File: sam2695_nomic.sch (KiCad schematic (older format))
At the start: 31 parts, among them J1 HeadphoneOut, J2 MicIn, U3 SAM2695, X1 12MHz

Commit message: UPDATEUPDATES!!!
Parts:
- removed C20: 1µfT, Capacitors_SMD:C_0805_HandSoldering, symbol Cap
- removed C21: 220pF, Capacitors_SMD:C_0805_HandSoldering, symbol C_Small
- removed J1: HeadphoneOut, Zetaohm:Switchcraft_3.5mm_SMD_Stereo, symbol Headphones-RESCUE-afx-01
- removed J2: MicIn, Zetaohm:Switchcraft_3.5mm_SMD_Stereo, symbol Headphones-RESCUE-afx-01
- removed R7: 4.7k, Resistors_SMD:R_0805_HandSoldering, symbol Resistor
- added U9: 3_pin_stereo, symbol 3_pin_stereo
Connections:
- net labels removed: VCC
- wire segments 136 -> 122
- no-connect marks 12 -> 10
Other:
- moved on the sheet: C12, R5
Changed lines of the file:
@@
 LIBS:contrib
 LIBS:valves
+LIBS:afx-01-cache
 EELAYER 25 0
 EELAYER END
@@
 $EndComp
 $Comp
-L VCC #PWR033
-U 1 1 55727FD6
-P 7650 4400
-F 0 "#PWR033" H 7650 4250 50  0001 C CNN
-F 1 "VCC" H 7650 4550 50  0000 C CNN
-F 2 "" H 7650 4400 60  0000 C CNN
-F 3 "" H 7650 4400 60  0000 C CNN
-	1    7650 4400
-	1    0    0    -1
-$EndComp
-$Comp
 L Cap C5
 U 1 1 55728143
@@
 $EndComp
 $Comp
-L VCC #PWR034
-U 1 1 55728291
-P 4250 3200
-F 0 "#PWR034" H 4250 3050 50  0001 C CNN
-F 1 "VCC" H 4250 3350 50  0000 C CNN
-F 2 "" H 4250 3200 60  0000 C CNN
-F 3 "" H 4250 3200 60  0000 C CNN
-	1    4250 3200
-	1    0    0    -1
-$EndComp
-$Comp
 L Cap C12
 U 1 1 55728514
-P 5800 2100
-F 0 "C12" V 5850 2200 39  0000 L CNN
-F 1 "100µfT" V 5650 2100 39  0000 L CNN
-F 2 "Capacitors_SMD:C_0805_HandSoldering" H 5710 2030 60  0001 C CNN
-F 3 "" H 5800 2100 60  0000 C CNN
-	1    5800 2100
+P 6100 1900
+F 0 "C12" V 6150 2000 39  0000 L CNN
+F 1 "100µfT" V 5950 1900 39  0000 L CNN
+F 2 "Capacitors_SMD:C_0805_HandSoldering" H 6010 1830 60  0001 C CNN
+F 3 "" H 6100 1900 60  0000 C CNN
+	1    6100 1900
 	0    -1   -1   0
 $EndComp
@@
 $EndComp
 $Comp
-L VCC #PWR035
-U 1 1 5572872F
-P 8050 3250
-F 0 "#PWR035" H 8050 3100 50  0001 C CNN
-F 1 "VCC" H 8050 3400 50  0000 C CNN
-F 2 "" H 8050 3250 60  0000 C CNN
-F 3 "" H 8050 3250 60  0000 C CNN
-	1    8050 3250
-	1    0    0    -1
-$EndComp
-$Comp
 L INDUCTOR_SMALL L1
 U 1 1 557287C4
@@
 L Resistor R5
 U 1 1 5572AB09
-P 7150 2200
-F 0 "R5" H 7300 2250 50  0000 C CNN
-F 1 "47k" H 7300 2150 50  0000 C CNN
-F 2 "Resistors_SMD:R_0805_HandSoldering" V 7080 2200 30  0001 C CNN
-F 3 "" H 7150 2200 30  0000 C CNN
-	1    7150 2200
-	1    0    0    -1
-$EndComp
-$Comp
-L Headphones-RESCUE-afx-01 J1
-U 1 1 5572B19C
-P 7750 1750
-F 0 "J1" H 7770 1900 60  0000 C CNN
-F 1 "HeadphoneOut" H 8000 1550 60  0000 C CNN
-F 2 "Zetaohm:Switchcraft_3.5mm_SMD_Stereo" H 7750 1750 60  0001 C CNN
-F 3 "" H 7750 1750 60  0000 C CNN
-	1    7750 1750
-	1    0    0    -1
-$EndComp
-$Comp
-L Headphones-RESCUE-afx-01 J2
-U 1 1 5572B6E6
-P 9050 2850
-F 0 "J2" H 9070 3000 60  0000 C CNN
-F 1 "MicIn" H 9150 2650 60  0000 C CNN
-F 2 "Zetaohm:Switchcraft_3.5mm_SMD_Stereo" H 9050 2850 60  0001 C CNN
-F 3 "" H 9050 2850 60  0000 C CNN
-	1    9050 2850
-	1    0    0    -1
-$EndComp
-$Comp
-L Cap C20
-U 1 1 5572BA3E
-P 7850 2750
-F 0 "C20" V 7900 2850 39  0000 L CNN
-F 1 "1µfT" V 7900 2250 39  0000 L CNN
-F 2 "Capacitors_SMD:C_0805_HandSoldering" H 7760 2680 60  0001 C CNN
-F 3 "" H 7850 2750 60  0000 C CNN
-	1    7850 2750
-	0    -1   -1   0
-$EndComp
-$Comp
-L C_Small C21
-U 1 1 5572BAE5
-P 8300 2850
-F 0 "C21" H 8450 2850 50  0000 L CNN
-F 1 "220pF" H 8350 2950 50  0000 L CNN
-F 2 "Capacitors_SMD:C_0805_HandSoldering" H 8300 2850 60  0001 C CNN
-F 3 "" H 8300 2850 60  0000 C CNN
-	1    8300 2850
-	-1   0    0    1
-$EndComp
-$Comp
-L Resistor R7
-U 1 1 5572BB93
-P 8500 3000
-F 0 "R7" H 8650 3050 50  0000 C CNN
-F 1 "4.7k" H 8650 2950 50  0000 C CNN
-F 2 "Resistors_SMD:R_0805_HandSoldering" V 8430 3000 30  0001 C CNN
-F 3 "" H 8500 3000 30  0000 C CNN
-	1    8500 3000
+P 6650 2000
+F 0 "R5" H 6800 2050 50  0000 C CNN
+F 1 "47k" H 6800 1950 50  0000 C CNN
+F 2 "Resistors_SMD:R_0805_HandSoldering" V 6580 2000 30  0001 C CNN
+F 3 "" H 6650 2000 30  0000 C CNN
+	1    6650 2000
 	1    0    0    -1
 $EndComp
 NoConn ~ 5350 3100
-NoConn ~ 7650 1700
-NoConn ~ 7650 1750
 Text HLabel 3550 2900 0    60   Input ~ 0
 MIDIIN
@@
 NoConn ~ 4650 4000
 $Comp
+L GNDA #PWR035
+U 1 1 561F077A
+P 6650 2350
+F 0 "#PWR035" H 6650 2100 50  0001 C CNN
+F 1 "GNDA" H 6650 2200 50  0000 C CNN
+F 2 "" H 6650 2350 60  0000 C CNN
+F 3 "" H 6650 2350 60  0000 C CNN
+	1    6650 2350
+	1    0    0    -1
+$EndComp
+$Comp
 L GNDA #PWR036
-U 1 1 561F077A
-P 7150 2400
-F 0 "#PWR036" H 7150 2150 50  0001 C CNN
-F 1 "GNDA" H 7150 2250 50  0000 C CNN
-F 2 "" H 7150 2400 60  0000 C CNN
-F 3 "" H 7150 2400 60  0000 C CNN
-	1    7150 2400
-	1    0    0    -1
-$EndComp
-$Comp
-L GNDA #PWR037
-U 1 1 561F07E6
-P 8850 3200
-F 0 "#PWR037" H 8850 2950 50  0001 C CNN
-F 1 "GNDA" H 8850 3050 50  0000 C CNN
-F 2 "" H 8850 3200 60  0000 C CNN
-F 3 "" H 8850 3200 60  0000 C CNN
-	1    8850 3200
-	1    0    0    -1
-$EndComp
-$Comp
-L GNDA #PWR038
-U 1 1 561F086A
-P 6250 1900
-F 0 "#PWR038" H 6250 1650 50  0001 C CNN
-F 1 "GNDA" H 6250 1750 50  0000 C CNN
-F 2 "" H 6250 1900 60  0000 C CNN
-F 3 "" H 6250 1900 60  0000 C CNN
-	1    6250 1900
-	1    0    0    -1
-$EndComp
-$Comp
-L GNDA #PWR039
 U 1 1 561F08CF
 P 8000 3600
-F 0 "#PWR039" H 8000 3350 50  0001 C CNN
+F 0 "#PWR036" H 8000 3350 50  0001 C CNN
 F 1 "GNDA" H 8000 3450 50  0000 C CNN
 F 2 "" H 8000 3600 60  0000 C CNN
@@
 $EndComp
 $Comp
-L GNDA #PWR040
+L GNDA #PWR037
 U 1 1 561F0AFD
 P 5400 5500
-F 0 "#PWR040" H 5400 5250 50  0001 C CNN
+F 0 "#PWR037" H 5400 5250 50  0001 C CNN
 F 1 "GNDA" H 5400 5350 50  0000 C CNN
 F 2 "" H 5400 5500 60  0000 C CNN
@@
 $EndComp
 $Comp
-L +3V3 #PWR041
+L +3V3 #PWR038
 U 1 1 561F0D6B
 P 4000 3600
-F 0 "#PWR041" H 4000 3450 50  0001 C CNN
+F 0 "#PWR038" H 4000 3450 50  0001 C CNN
 F 1 "+3V3" H 4000 3740 50  0000 C CNN
 F 2 "" H 4000 3600 60  0000 C CNN
@@
 Connection ~ 6800 4200
 Wire Wire Line
-	4500 5350 4500 5100
-Wire Wire Line
-	4500 5100 4650 5100
+	4550 5350 4550 4500
+Wire Wire Line
+	4550 5100 4650 5100
 Connection ~ 7450 4350
 Wire Wire Line
-	4650 4500 4550 4500
-Wire Wire Line
-	4550 4500 4550 5100
+	4550 4500 4650 4500
 Wire Wire Line
 	4550 4600 4650 4600
@@
 Wire Wire Line
 	7650 4450 7650 4400
-Connection ~ 4500 5350
+Connection ~ 4550 5350
 Wire Wire Line
 	4650 3250 4250 3250
@@
 	5550 2900 5350 2900
 Wire Wire Line
-	5550 2100 5550 2900
-Wire Wire Line
-	5550 2100 5700 2100
+	5550 1900 5550 2900
+Wire Wire Line
+	5550 1900 6000 1900
 Wire Wire Line
 	5400 1650 5400 3000
@@
 	5850 1650 7650 1650
 Wire Wire Line
-	6250 1850 6250 1900
-Wire Wire Line
-	5850 2100 7500 2100
-Wire Wire Line
-	7150 2300 7150 2400
+	6250 1850 6250 2200
+Wire Wire Line
+	6150 1900 7050 1900
+Wire Wire Line
+	6650 2100 6650 2350
 Connection ~ 6250 1650
 Wire Wire Line
-	7500 2100 7500 1800
-Wire Wire Line
-	7500 1800 7650 1800
-Connection ~ 7150 2100
-Wire Wire Line
-	7650 1850 7600 1850
-Wire Wire Line
-	7600 1850 7600 2350
-Wire Wire Line
-	7600 2350 7150 2350
-Connection ~ 7150 2350
-Wire Wire Line
-	5350 3200 5800 3200
-Wire Wire Line
-	5800 3200 5800 2750
-Wire Wire Line
-	5800 2750 7750 2750
-Wire Wire Line
-	8950 2900 8500 2900
-Wire Wire Line
-	8850 2950 8950 2950
-Wire Wire Line
-	8850 2750 8850 3200
-Wire Wire Line
-	8300 3100 8850 3100
-Connection ~ 8850 3100
-Wire Wire Line
-	8300 3100 8300 2950
-Connection ~ 8500 3100
-Wire Wire Line
-	7900 2750 8500 2750
-Wire Wire Line
-	8500 2750 8500 2900
-Connection ~ 8300 2750
-Wire Wire Line
-	8850 2750 8950 2750
-Connection ~ 8850 2950
-Wire Wire Line
-	8950 2800 8850 2800
-Connection ~ 8850 2800
-Wire Wire Line
-	8950 2850 8850 2850
-Connection ~ 8850 2850
+	7050 1900 7050 1750
+Wire Wire Line
+	7050 1750 7650 1750
+Connection ~ 6650 1900
+Wire Wire Line
+	7650 1850 7200 1850
+Wire Wire Line
+	7200 1850 7200 2200
+Wire Wire Line
+	7200 2200 6250 2200
+Connection ~ 6650 2200
 Wire Wire Line
 	3550 2900 3850 2900
@@
 Connection ~ 4000 4250
 Connection ~ 4000 4150
+$Comp
+L 3_pin_stereo U9
+U 1 1 5622F23F
+P 7750 1750
+F 0 "U9" H 7770 1900 60  0000 C CNN
+F 1 "3_pin_stereo" H 7920 1600 60  0000 C CNN
+F 2 "" H 7750 1750 60  0000 C CNN
+F 3 "" H 7750 1750 60  0000 C CNN
+	1    7750 1750
+	1    0    0    -1
+$EndComp
+$Comp
+L +3V3 #PWR039
+U 1 1 5622FC98
+P 4250 3200
+F 0 "#PWR039" H 4250 3050 50  0001 C CNN
+F 1 "+3V3" H 4250 3340 50  0000 C CNN
+F 2 "" H 4250 3200 60  0000 C CNN
+F 3 "" H 4250 3200 60  0000 C CNN
+	1    4250 3200
+	1    0    0    -1
+$EndComp
+$Comp
+L +3V3 #PWR040
+U 1 1 5622FD5B
+P 7650 4400
+F 0 "#PWR040" H 7650 4250 50  0001 C CNN
+F 1 "+3V3" H 7650 4540 50  0000 C CNN
+F 2 "" H 7650 4400 60  0000 C CNN
+F 3 "" H 7650 4400 60  0000 C CNN
+	1    7650 4400
+	1    0    0    -1
+$EndComp
+$Comp
+L +3V3 #PWR041
+U 1 1 5622FDB4
+P 8050 3250
+F 0 "#PWR041" H 8050 3100 50  0001 C CNN
+F 1 "+3V3" H 8050 3390 50  0000 C CNN
+F 2 "" H 8050 3250 60  0000 C CNN
+F 3 "" H 8050 3250 60  0000 C CNN
+	1    8050 3250
+	1    0    0    -1
+$EndComp
 $EndSCHEMATC

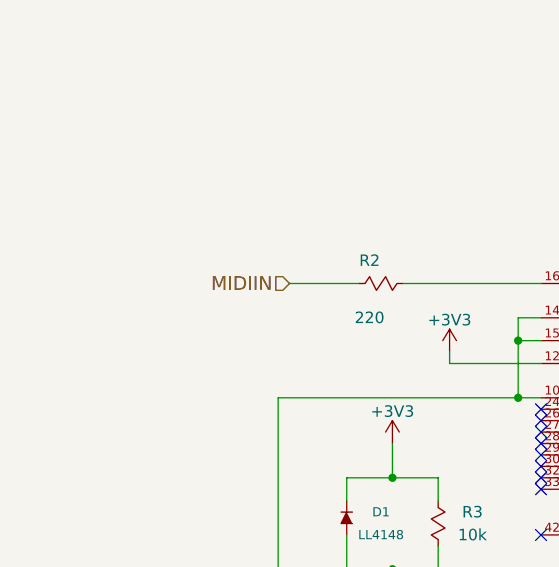
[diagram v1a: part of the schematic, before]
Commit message: Added Touch Capacitive Panel
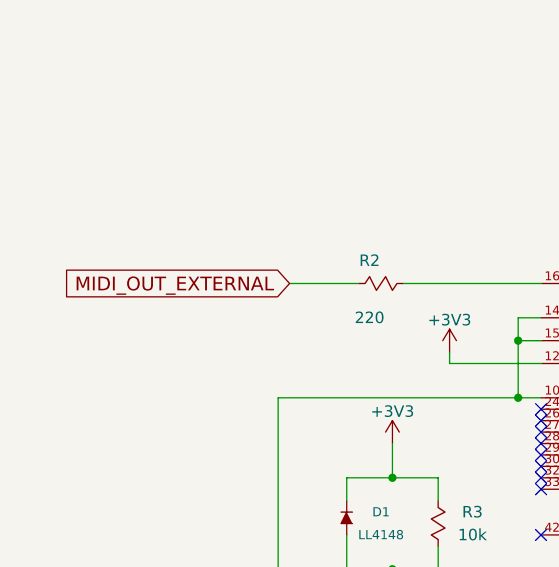
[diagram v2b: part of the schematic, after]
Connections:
- net MIDIIN renamed MIDI_OUT_EXTERNAL
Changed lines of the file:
@@
 $Descr A4 11693 8268
 encoding utf-8
-Sheet 3 7
+Sheet 3 8
 Title ""
 Date ""
@@
 $EndComp
 NoConn ~ 5350 3100
-Text HLabel 3550 2900 0    60   Input ~ 0
-MIDIIN
 $Comp
 L Resistor R2
@@
 NoConn ~ 4650 4000
 $Comp
-L GNDA #PWR035
+L GNDA #PWR037
 U 1 1 561F077A
 P 6650 2350
-F 0 "#PWR035" H 6650 2100 50  0001 C CNN
+F 0 "#PWR037" H 6650 2100 50  0001 C CNN
 F 1 "GNDA" H 6650 2200 50  0000 C CNN
 F 2 "" H 6650 2350 60  0000 C CNN
@@
 $EndComp
 $Comp
-L GNDA #PWR036
+L GNDA #PWR038
 U 1 1 561F08CF
 P 8000 3600
-F 0 "#PWR036" H 8000 3350 50  0001 C CNN
+F 0 "#PWR038" H 8000 3350 50  0001 C CNN
 F 1 "GNDA" H 8000 3450 50  0000 C CNN
 F 2 "" H 8000 3600 60  0000 C CNN
@@
 $EndComp
 $Comp
-L GNDA #PWR037
+L GNDA #PWR039
 U 1 1 561F0AFD
 P 5400 5500
-F 0 "#PWR037" H 5400 5250 50  0001 C CNN
+F 0 "#PWR039" H 5400 5250 50  0001 C CNN
 F 1 "GNDA" H 5400 5350 50  0000 C CNN
 F 2 "" H 5400 5500 60  0000 C CNN
@@
 $EndComp
 $Comp
-L +3V3 #PWR038
+L +3V3 #PWR040
 U 1 1 561F0D6B
 P 4000 3600
-F 0 "#PWR038" H 4000 3450 50  0001 C CNN
+F 0 "#PWR040" H 4000 3450 50  0001 C CNN
 F 1 "+3V3" H 4000 3740 50  0000 C CNN
 F 2 "" H 4000 3600 60  0000 C CNN
@@
 $EndComp
 $Comp
-L +3V3 #PWR039
+L +3V3 #PWR041
 U 1 1 5622FC98
 P 4250 3200
-F 0 "#PWR039" H 4250 3050 50  0001 C CNN
+F 0 "#PWR041" H 4250 3050 50  0001 C CNN
 F 1 "+3V3" H 4250 3340 50  0000 C CNN
 F 2 "" H 4250 3200 60  0000 C CNN
@@
 $EndComp
 $Comp
-L +3V3 #PWR040
+L +3V3 #PWR042
 U 1 1 5622FD5B
 P 7650 4400
-F 0 "#PWR040" H 7650 4250 50  0001 C CNN
+F 0 "#PWR042" H 7650 4250 50  0001 C CNN
 F 1 "+3V3" H 7650 4540 50  0000 C CNN
 F 2 "" H 7650 4400 60  0000 C CNN
@@
 $EndComp
 $Comp
-L +3V3 #PWR041
+L +3V3 #PWR043
 U 1 1 5622FDB4
 P 8050 3250
-F 0 "#PWR041" H 8050 3100 50  0001 C CNN
+F 0 "#PWR043" H 8050 3100 50  0001 C CNN
 F 1 "+3V3" H 8050 3390 50  0000 C CNN
 F 2 "" H 8050 3250 60  0000 C CNN
@@
 	1    0    0    -1
 $EndComp
+Text GLabel 3550 2900 0    60   Input ~ 0
+MIDI_OUT_EXTERNAL
 $EndSCHEMATC

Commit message: Updating footprints
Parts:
- C10, C11, C12, C13, C14, C15, C16, C17, C18, C19, C25, C26, C5, C6, C7, C8, C9: footprint Capacitors_SMD:C_0805_HandSoldering -> Capacitors_SMD:C_0603_HandSoldering
- R2, R3, R4, R5, R6: footprint Resistors_SMD:R_0805_HandSoldering -> Resistors_SMD:R_0603_HandSoldering
- U9: footprint (none) -> Zetaohm:KOBICONN_ST
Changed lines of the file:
@@
 $Descr A4 11693 8268
 encoding utf-8
-Sheet 3 8
+Sheet 3 7
 Title ""
 Date ""
@@
 F 0 "C14" V 6200 5050 39  0000 L CNN
 F 1 "22pF" V 6050 4950 39  0000 L CNN
-F 2 "Capacitors_SMD:C_0805_HandSoldering" H 6060 4930 60  0001 C CNN
+F 2 "Capacitors_SMD:C_0603_HandSoldering" H 6060 4930 60  0001 C CNN
 F 3 "" H 6150 5000 60  0000 C CNN
 	1    6150 5000
@@
 F 0 "C13" V 6200 4750 39  0000 L CNN
 F 1 "22pF" V 6050 4700 39  0000 L CNN
-F 2 "Capacitors_SMD:C_0805_HandSoldering" H 6060 4630 60  0001 C CNN
+F 2 "Capacitors_SMD:C_0603_HandSoldering" H 6060 4630 60  0001 C CNN
 F 3 "" H 6150 4700 60  0000 C CNN
 	1    6150 4700
@@
 F 0 "C17" V 6300 3900 39  0000 L CNN
 F 1 "10µfT" V 6300 3300 39  0000 L CNN
-F 2 "Capacitors_SMD:C_0805_HandSoldering" H 6160 3730 60  0001 C CNN
+F 2 "Capacitors_SMD:C_0603_HandSoldering" H 6160 3730 60  0001 C CNN
 F 3 "" H 6250 3800 60  0000 C CNN
 	1    6250 3800
@@
 F 0 "C6" V 5650 3750 50  0000 L CNN
 F 1 "100nF" V 5650 4000 50  0000 L CNN
-F 2 "Capacitors_SMD:C_0805_HandSoldering" H 5700 3700 60  0001 C CNN
+F 2 "Capacitors_SMD:C_0603_HandSoldering" H 5700 3700 60  0001 C CNN
 F 3 "" H 5700 3700 60  0000 C CNN
 	1    5700 3700
@@
 F 0 "C7" V 5650 3950 50  0000 L CNN
 F 1 "100nF" V 5650 4200 50  0000 L CNN
-F 2 "Capacitors_SMD:C_0805_HandSoldering" H 5700 3900 60  0001 C CNN
+F 2 "Capacitors_SMD:C_0603_HandSoldering" H 5700 3900 60  0001 C CNN
 F 3 "" H 5700 3900 60  0000 C CNN
 	1    5700 3900
@@
 F 0 "C10" V 5650 4400 50  0000 L CNN
 F 1 "100nF" V 5650 4650 50  0000 L CNN
-F 2 "Capacitors_SMD:C_0805_HandSoldering" H 5700 4350 60  0001 C CNN
+F 2 "Capacitors_SMD:C_0603_HandSoldering" H 5700 4350 60  0001 C CNN
 F 3 "" H 5700 4350 60  0000 C CNN
 	1    5700 4350
@@
 F 0 "C8" V 5650 4100 50  0000 L CNN
 F 1 "100nF" V 5650 4350 50  0000 L CNN
-F 2 "Capacitors_SMD:C_0805_HandSoldering" H 5700 4050 60  0001 C CNN
+F 2 "Capacitors_SMD:C_0603_HandSoldering" H 5700 4050 60  0001 C CNN
 F 3 "" H 5700 4050 60  0000 C CNN
 	1    5700 4050
@@
 F 0 "C9" V 5650 4250 50  0000 L CNN
 F 1 "100nF" V 5650 4500 50  0000 L CNN
-F 2 "Capacitors_SMD:C_0805_HandSoldering" H 5700 4200 60  0001 C CNN
+F 2 "Capacitors_SMD:C_0603_HandSoldering" H 5700 4200 60  0001 C CNN
 F 3 "" H 5700 4200 60  0000 C CNN
 	1    5700 4200
@@
 F 0 "R3" H 4350 4000 50  0000 C CNN
 F 1 "10k" H 4350 3900 50  0000 C CNN
-F 2 "Resistors_SMD:R_0805_HandSoldering" V 4130 3950 30  0001 C CNN
+F 2 "Resistors_SMD:R_0603_HandSoldering" V 4130 3950 30  0001 C CNN
 F 3 "" H 4200 3950 30  0000 C CNN
 	1    4200 3950
@@
 F 0 "C5" H 4150 4750 39  0000 L CNN
 F 1 "1µfT" H 4150 4650 39  0000 L CNN
-F 2 "Capacitors_SMD:C_0805_HandSoldering" H 3910 4730 60  0001 C CNN
+F 2 "Capacitors_SMD:C_0603_HandSoldering" H 3910 4730 60  0001 C CNN
 F 3 "" H 4000 4800 60  0000 C CNN
 	1    4000 4800
@@
 F 0 "C12" V 6150 2000 39  0000 L CNN
 F 1 "100µfT" V 5950 1900 39  0000 L CNN
-F 2 "Capacitors_SMD:C_0805_HandSoldering" H 6010 1830 60  0001 C CNN
+F 2 "Capacitors_SMD:C_0603_HandSoldering" H 6010 1830 60  0001 C CNN
 F 3 "" H 6100 1900 60  0000 C CNN
 	1    6100 1900
@@
 F 0 "R4" H 6400 1800 50  0000 C CNN
 F 1 "47k" H 6400 1700 50  0000 C CNN
-F 2 "Resistors_SMD:R_0805_HandSoldering" V 6180 1750 30  0001 C CNN
+F 2 "Resistors_SMD:R_0603_HandSoldering" V 6180 1750 30  0001 C CNN
 F 3 "" H 6250 1750 30  0000 C CNN
 	1    6250 1750
@@
 F 0 "C18" V 7050 3500 50  0000 L CNN
 F 1 "100nF" V 7050 3800 50  0000 L CNN
-F 2 "Capacitors_SMD:C_0805_HandSoldering" H 7100 3450 60  0001 C CNN
+F 2 "Capacitors_SMD:C_0603_HandSoldering" H 7100 3450 60  0001 C CNN
 F 3 "" H 7100 3450 60  0000 C CNN
 	1    7100 3450
@@
 F 0 "C19" V 7300 3700 39  0000 L CNN
 F 1 "10µfT" V 7300 3100 39  0000 L CNN
-F 2 "Capacitors_SMD:C_0805_HandSoldering" H 7160 3530 60  0001 C CNN
+F 2 "Capacitors_SMD:C_0603_HandSoldering" H 7160 3530 60  0001 C CNN
 F 3 "" H 7250 3600 60  0000 C CNN
 	1    7250 3600
@@
 F 0 "R6" H 7600 3900 50  0000 C CNN
 F 1 "0" H 7600 3800 50  0000 C CNN
-F 2 "Resistors_SMD:R_0805_HandSoldering" V 7680 3850 30  0001 C CNN
+F 2 "Resistors_SMD:R_0603_HandSoldering" V 7680 3850 30  0001 C CNN
 F 3 "" H 7750 3850 30  0000 C CNN
 	1    7750 3850
@@
 F 0 "C16" V 6300 3250 39  0000 L CNN
 F 1 "10µfT" V 6300 2650 39  0000 L CNN
-F 2 "Capacitors_SMD:C_0805_HandSoldering" H 6160 3080 60  0001 C CNN
+F 2 "Capacitors_SMD:C_0603_HandSoldering" H 6160 3080 60  0001 C CNN
 F 3 "" H 6250 3150 60  0000 C CNN
 	1    6250 3150
@@
 F 0 "C11" V 5850 1750 39  0000 L CNN
 F 1 "100µfT" V 5650 1650 39  0000 L CNN
-F 2 "Capacitors_SMD:C_0805_HandSoldering" H 5710 1580 60  0001 C CNN
+F 2 "Capacitors_SMD:C_0603_HandSoldering" H 5710 1580 60  0001 C CNN
 F 3 "" H 5800 1650 60  0000 C CNN
 	1    5800 1650
@@
 F 0 "C15" V 6150 3000 50  0000 L CNN
 F 1 "100nF" V 6150 3250 50  0000 L CNN
-F 2 "Capacitors_SMD:C_0805_HandSoldering" H 6200 2950 60  0001 C CNN
+F 2 "Capacitors_SMD:C_0603_HandSoldering" H 6200 2950 60  0001 C CNN
 F 3 "" H 6200 2950 60  0000 C CNN
 	1    6200 2950
@@
 F 0 "R5" H 6800 2050 50  0000 C CNN
 F 1 "47k" H 6800 1950 50  0000 C CNN
-F 2 "Resistors_SMD:R_0805_HandSoldering" V 6580 2000 30  0001 C CNN
+F 2 "Resistors_SMD:R_0603_HandSoldering" V 6580 2000 30  0001 C CNN
 F 3 "" H 6650 2000 30  0000 C CNN
 	1    6650 2000
@@
 F 0 "R2" V 3850 2850 50  0000 C CNN
 F 1 "220" V 4100 2850 50  0000 C CNN
-F 2 "Resistors_SMD:R_0805_HandSoldering" V 3880 2900 30  0001 C CNN
+F 2 "Resistors_SMD:R_0603_HandSoldering" V 3880 2900 30  0001 C CNN
 F 3 "" H 3950 2900 30  0000 C CNN
 	1    3950 2900
@@
 F 0 "C25" V 6850 4750 39  0000 L CNN
 F 1 "4.7µfT" V 6850 4150 39  0000 L CNN
-F 2 "Capacitors_SMD:C_0805_HandSoldering" H 6710 4580 60  0001 C CNN
+F 2 "Capacitors_SMD:C_0603_HandSoldering" H 6710 4580 60  0001 C CNN
 F 3 "" H 6800 4650 60  0000 C CNN
 	1    6800 4650
@@
 F 0 "C26" V 6750 4950 50  0000 L CNN
 F 1 "100nF" V 6750 5250 50  0000 L CNN
-F 2 "Capacitors_SMD:C_0805_HandSoldering" H 6800 4900 60  0001 C CNN
+F 2 "Capacitors_SMD:C_0603_HandSoldering" H 6800 4900 60  0001 C CNN
 F 3 "" H 6800 4900 60  0000 C CNN
 	1    6800 4900
@@
 F 0 "U9" H 7770 1900 60  0000 C CNN
 F 1 "3_pin_stereo" H 7920 1600 60  0000 C CNN
-F 2 "" H 7750 1750 60  0000 C CNN
+F 2 "Zetaohm:KOBICONN_ST" H 7750 1750 60  0001 C CNN
 F 3 "" H 7750 1750 60  0000 C CNN
 	1    7750 1750

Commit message: Small updates
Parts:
- C11, C12, C16, C17, C19, C25, C5: footprint Capacitors_SMD:C_0603_HandSoldering -> Capacitors_Tantalum_SMD:TantalC_SizeA_EIA-3216_HandSoldering
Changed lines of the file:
@@
 F 0 "C17" V 6300 3900 39  0000 L CNN
 F 1 "10µfT" V 6300 3300 39  0000 L CNN
-F 2 "Capacitors_SMD:C_0603_HandSoldering" H 6160 3730 60  0001 C CNN
+F 2 "Capacitors_Tantalum_SMD:TantalC_SizeA_EIA-3216_HandSoldering" H 6160 3730 60  0001 C CNN
 F 3 "" H 6250 3800 60  0000 C CNN
 	1    6250 3800
@@
 F 0 "C5" H 4150 4750 39  0000 L CNN
 F 1 "1µfT" H 4150 4650 39  0000 L CNN
-F 2 "Capacitors_SMD:C_0603_HandSoldering" H 3910 4730 60  0001 C CNN
+F 2 "Capacitors_Tantalum_SMD:TantalC_SizeA_EIA-3216_HandSoldering" H 3910 4730 60  0001 C CNN
 F 3 "" H 4000 4800 60  0000 C CNN
 	1    4000 4800
@@
 F 0 "C12" V 6150 2000 39  0000 L CNN
 F 1 "100µfT" V 5950 1900 39  0000 L CNN
-F 2 "Capacitors_SMD:C_0603_HandSoldering" H 6010 1830 60  0001 C CNN
+F 2 "Capacitors_Tantalum_SMD:TantalC_SizeA_EIA-3216_HandSoldering" H 6010 1830 60  0001 C CNN
 F 3 "" H 6100 1900 60  0000 C CNN
 	1    6100 1900
@@
 F 0 "C19" V 7300 3700 39  0000 L CNN
 F 1 "10µfT" V 7300 3100 39  0000 L CNN
-F 2 "Capacitors_SMD:C_0603_HandSoldering" H 7160 3530 60  0001 C CNN
+F 2 "Capacitors_Tantalum_SMD:TantalC_SizeA_EIA-3216_HandSoldering" H 7160 3530 60  0001 C CNN
 F 3 "" H 7250 3600 60  0000 C CNN
 	1    7250 3600
@@
 F 0 "C16" V 6300 3250 39  0000 L CNN
 F 1 "10µfT" V 6300 2650 39  0000 L CNN
-F 2 "Capacitors_SMD:C_0603_HandSoldering" H 6160 3080 60  0001 C CNN
+F 2 "Capacitors_Tantalum_SMD:TantalC_SizeA_EIA-3216_HandSoldering" H 6160 3080 60  0001 C CNN
 F 3 "" H 6250 3150 60  0000 C CNN
 	1    6250 3150
@@
 F 0 "C11" V 5850 1750 39  0000 L CNN
 F 1 "100µfT" V 5650 1650 39  0000 L CNN
-F 2 "Capacitors_SMD:C_0603_HandSoldering" H 5710 1580 60  0001 C CNN
+F 2 "Capacitors_Tantalum_SMD:TantalC_SizeA_EIA-3216_HandSoldering" H 5710 1580 60  0001 C CNN
 F 3 "" H 5800 1650 60  0000 C CNN
 	1    5800 1650
@@
 F 0 "C25" V 6850 4750 39  0000 L CNN
 F 1 "4.7µfT" V 6850 4150 39  0000 L CNN
-F 2 "Capacitors_SMD:C_0603_HandSoldering" H 6710 4580 60  0001 C CNN
+F 2 "Capacitors_Tantalum_SMD:TantalC_SizeA_EIA-3216_HandSoldering" H 6710 4580 60  0001 C CNN
 F 3 "" H 6800 4650 60  0000 C CNN
 	1    6800 4650
